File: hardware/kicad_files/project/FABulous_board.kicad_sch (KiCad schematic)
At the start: 7 parts, among them SW1 Tactile Switch

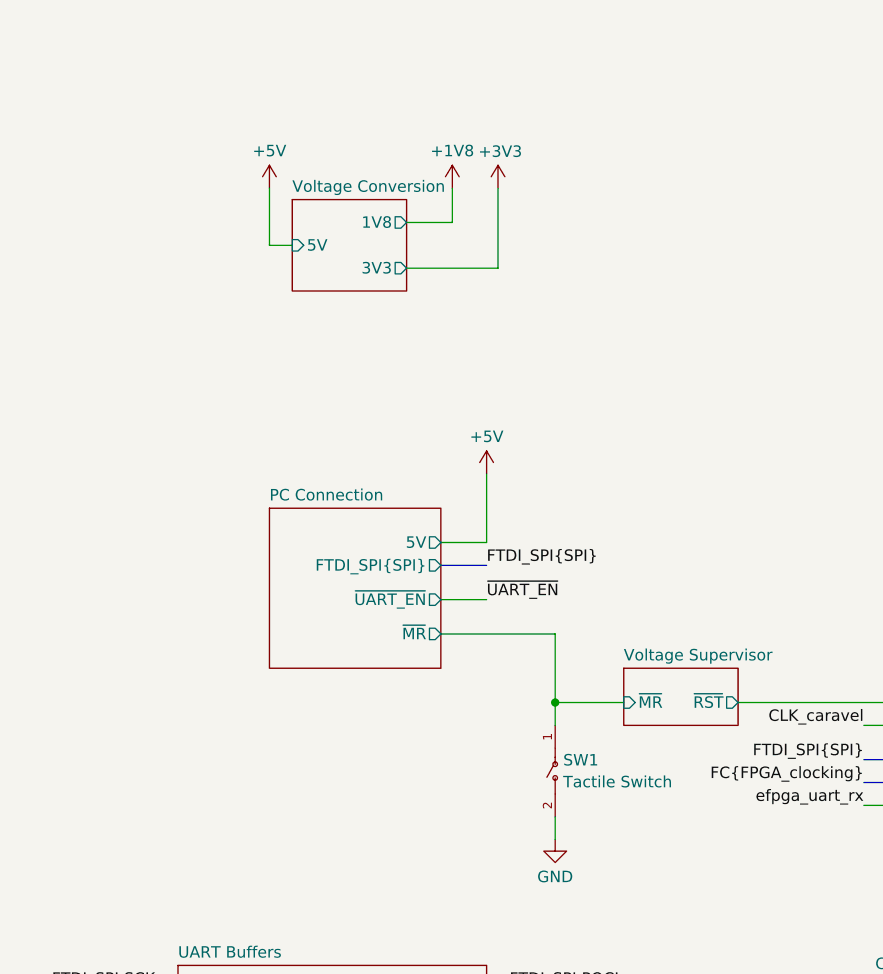
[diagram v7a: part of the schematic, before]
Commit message: fix: replace all local symbols and footprints with versions from KiCad or project libraries
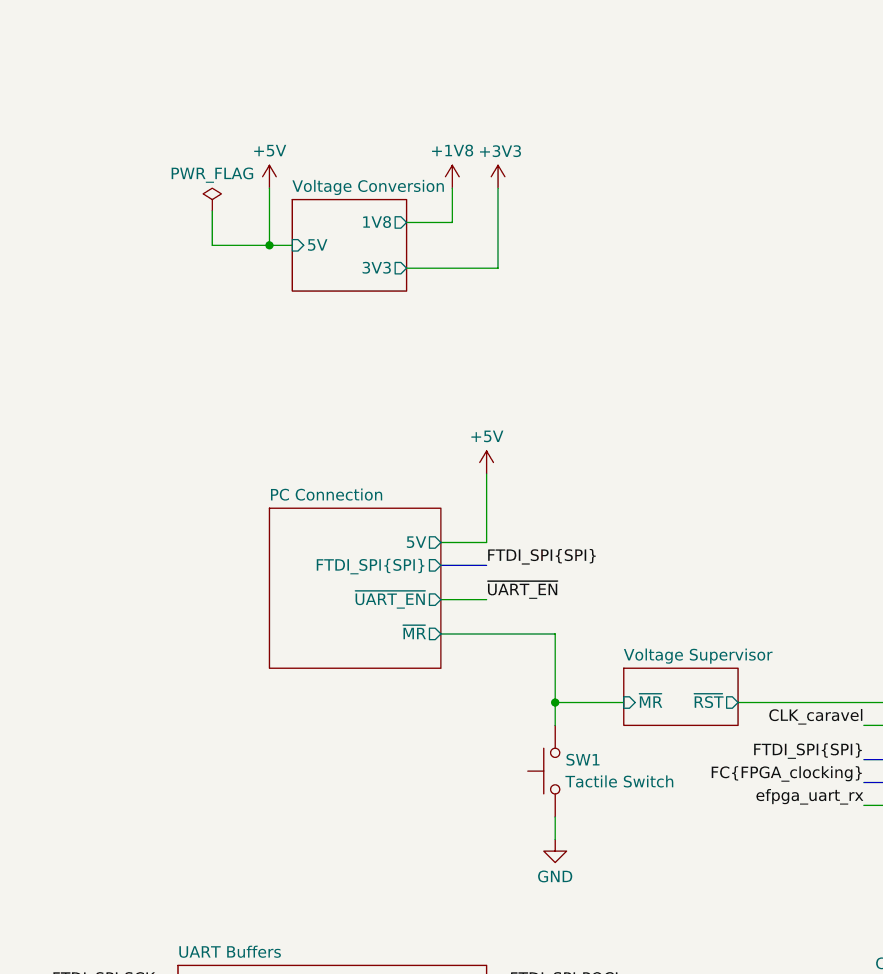
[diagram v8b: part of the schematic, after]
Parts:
- D2: footprint easy_eda:LED1206-R-RD_RED -> LED_SMD:LED_1206_3216Metric
- SW1: footprint easy_eda:SW_SMD_4P_L6.0_W6.0-P4.5-LS8.6 -> Button_Switch_SMD:SW_SPST_Omron_B3FS-101xP; symbol easy_eda:Tactile Switch -> Switch:SW_Push
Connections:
- net GND: now also SW1.1; no longer SW1.2, SW1.4
- net PC Connection/~{MR}: now also SW1.2; no longer SW1.1, SW1.3
